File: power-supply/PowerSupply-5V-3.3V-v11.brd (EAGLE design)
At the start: 31.8 x 31.8 mm, 19 parts, among them J1 POWER_JACK, J3 VCC, J4 GND, J5 NC1, J6 NC2, U1 LM317

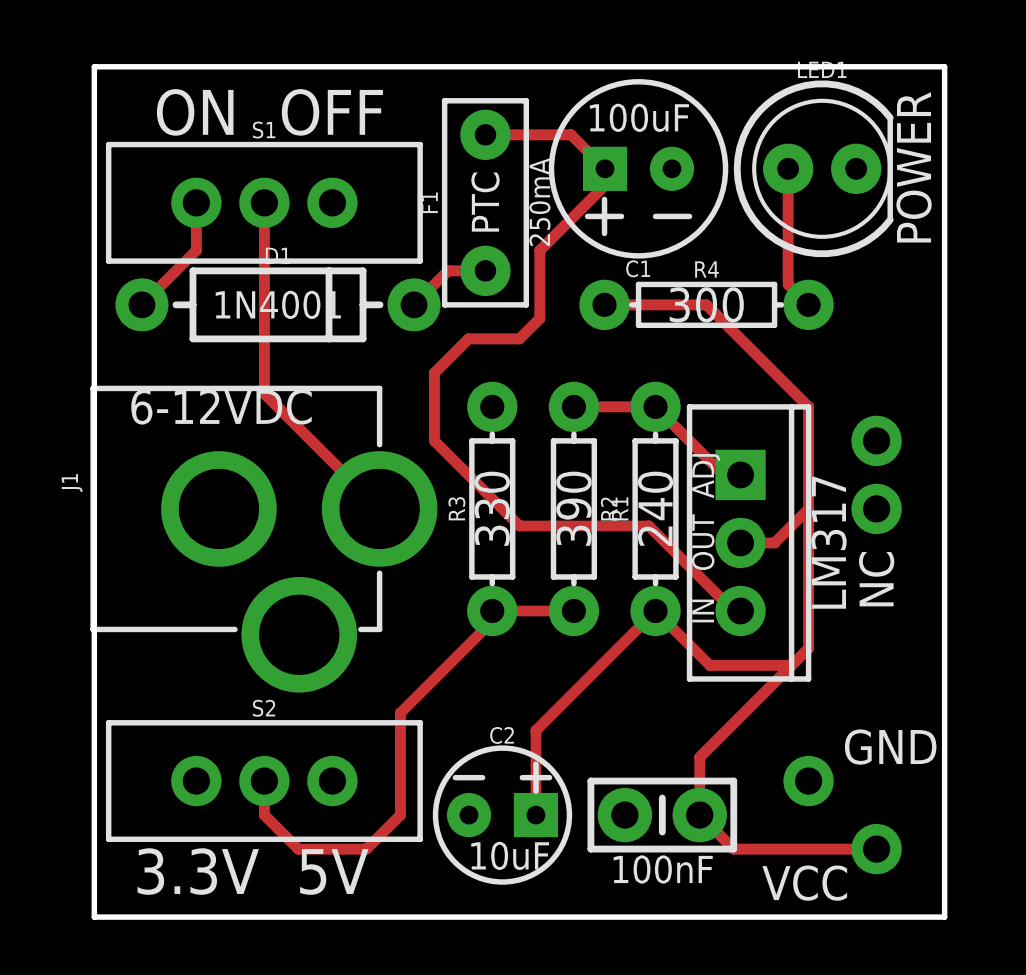
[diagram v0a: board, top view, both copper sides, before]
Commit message: Add raw voltage source
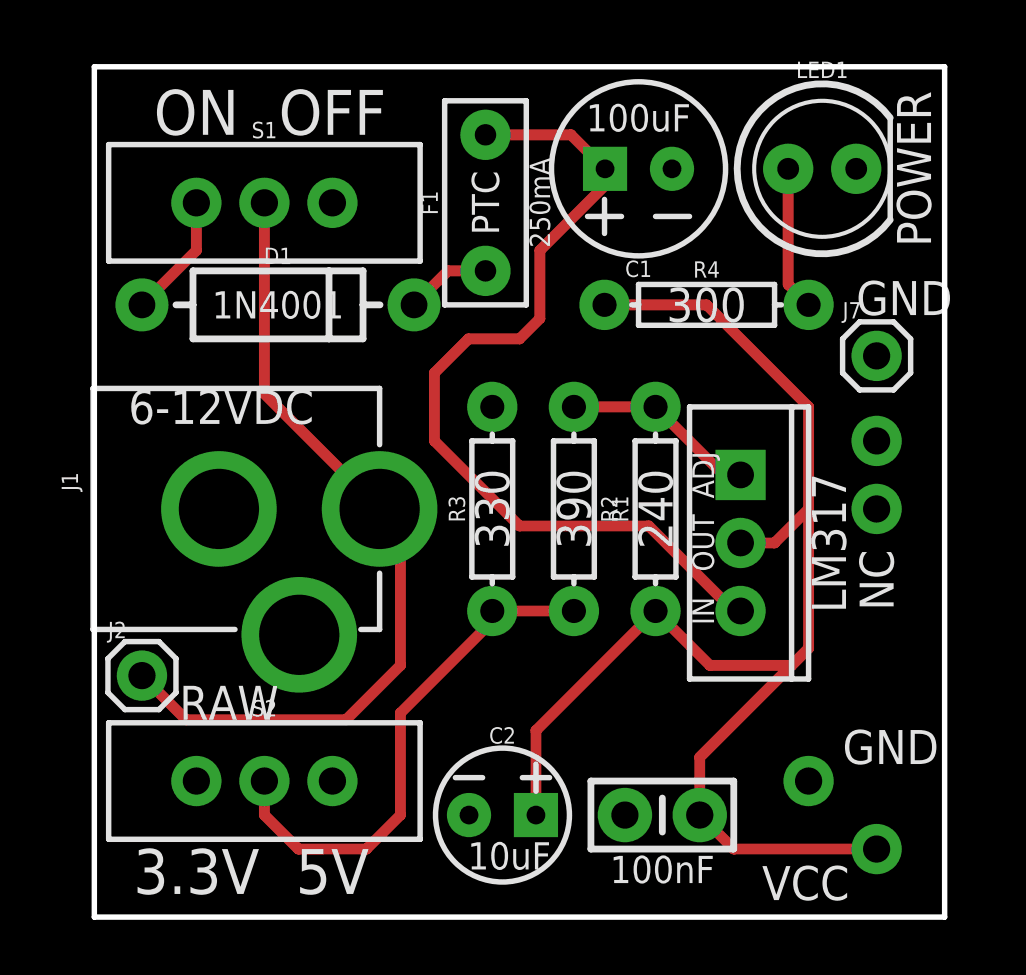
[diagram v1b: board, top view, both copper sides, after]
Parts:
- added J2: RAW, SparkFun-Connectors:1X01
- added J7: GND, SparkFun-Connectors:1X01
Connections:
- net GND: now also J7.1
- net VIN: now also J2.1
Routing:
- net VIN: track 13.2 -> 30.6 mm
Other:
- board text added: "RAW"
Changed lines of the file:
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@@
 <text x="22.733" y="11.43" size="0.8128" layer="21" font="vector" ratio="12" rot="R270" align="center">IN</text>
 <text x="27.432" y="13.97" size="1.27" layer="21" font="vector" ratio="12" rot="R270" align="center">LM317</text>
+<text x="3.175" y="7.366" size="1.27" layer="21" font="vector">RAW</text>
+<text x="28.448" y="22.479" size="1.27" layer="21" font="vector">GND</text>
 </plain>
 <attributes>
@@
 <element name="J5" library="SparkFun-Connectors" package="1X01" value="NC1" x="29.21" y="15.24" rot="MR90"/>
 <element name="J6" library="SparkFun-Connectors" package="1X01" value="NC2" x="29.21" y="17.78" rot="MR90"/>
+<element name="J2" library="SparkFun-Connectors" package="1X01" value="RAW" x="1.778" y="9.017"/>
+<element name="J7" library="SparkFun-Connectors" package="1X01" value="GND" x="29.21" y="20.955"/>
 </elements>
 <signals>
@@
 <contactref element="J1" pad="PWR"/>
 <contactref element="S1" pad="2"/>
-<wire x1="10.652" y1="15.24" x2="6.35" y2="19.542" width="0.4064" layer="1"/>
+<wire x1="6.35" y1="19.542" x2="10.652" y2="15.24" width="0.4064" layer="1"/>
 <wire x1="6.35" y1="19.542" x2="6.35" y2="26.67" width="0.4064" layer="1"/>
+<contactref element="J2" pad="1"/>
+<wire x1="10.652" y1="15.24" x2="11.43" y2="14.462" width="0.4064" layer="1"/>
+<wire x1="11.43" y1="9.398" x2="9.398" y2="7.366" width="0.4064" layer="1"/>
+<wire x1="9.398" y1="7.366" x2="3.429" y2="7.366" width="0.4064" layer="1"/>
+<wire x1="3.429" y1="7.366" x2="1.778" y2="9.017" width="0.4064" layer="1"/>
+<wire x1="11.43" y1="14.462" x2="11.43" y2="9.398" width="0.4064" layer="1"/>
 </signal>
 <signal name="GND">
@@
 <vertex x="31.75" y="0"/>
 </polygon>
+<contactref element="J7" pad="1"/>
 </signal>
 <signal name="ON">
